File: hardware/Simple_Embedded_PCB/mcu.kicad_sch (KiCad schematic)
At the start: 26 parts, among them J1 USB_B_Micro, J2 SWD Connector, J3 Conn_01x09, J4 Conn_01x09, J5 Conn_01x09, J6 Conn_01x09, Q1 AO3400A, U1 STM32F103C8Tx, X1 SG-8018CE 8.000000MHz

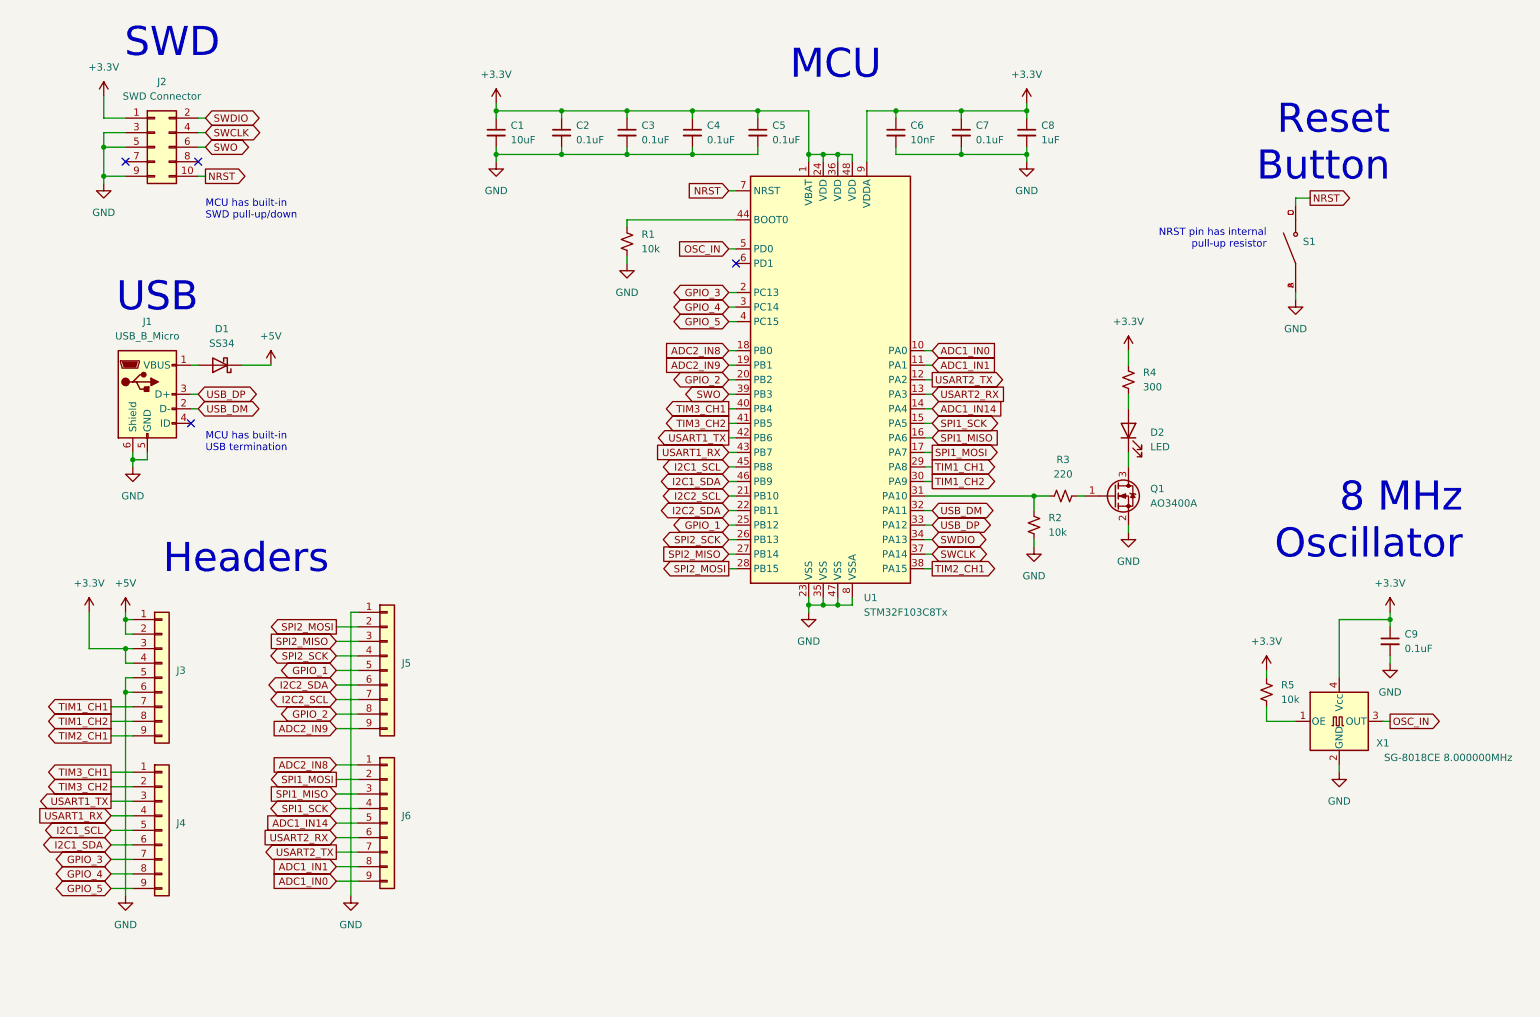
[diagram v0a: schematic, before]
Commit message: Added 4.7k pullups to I2C and reannotated
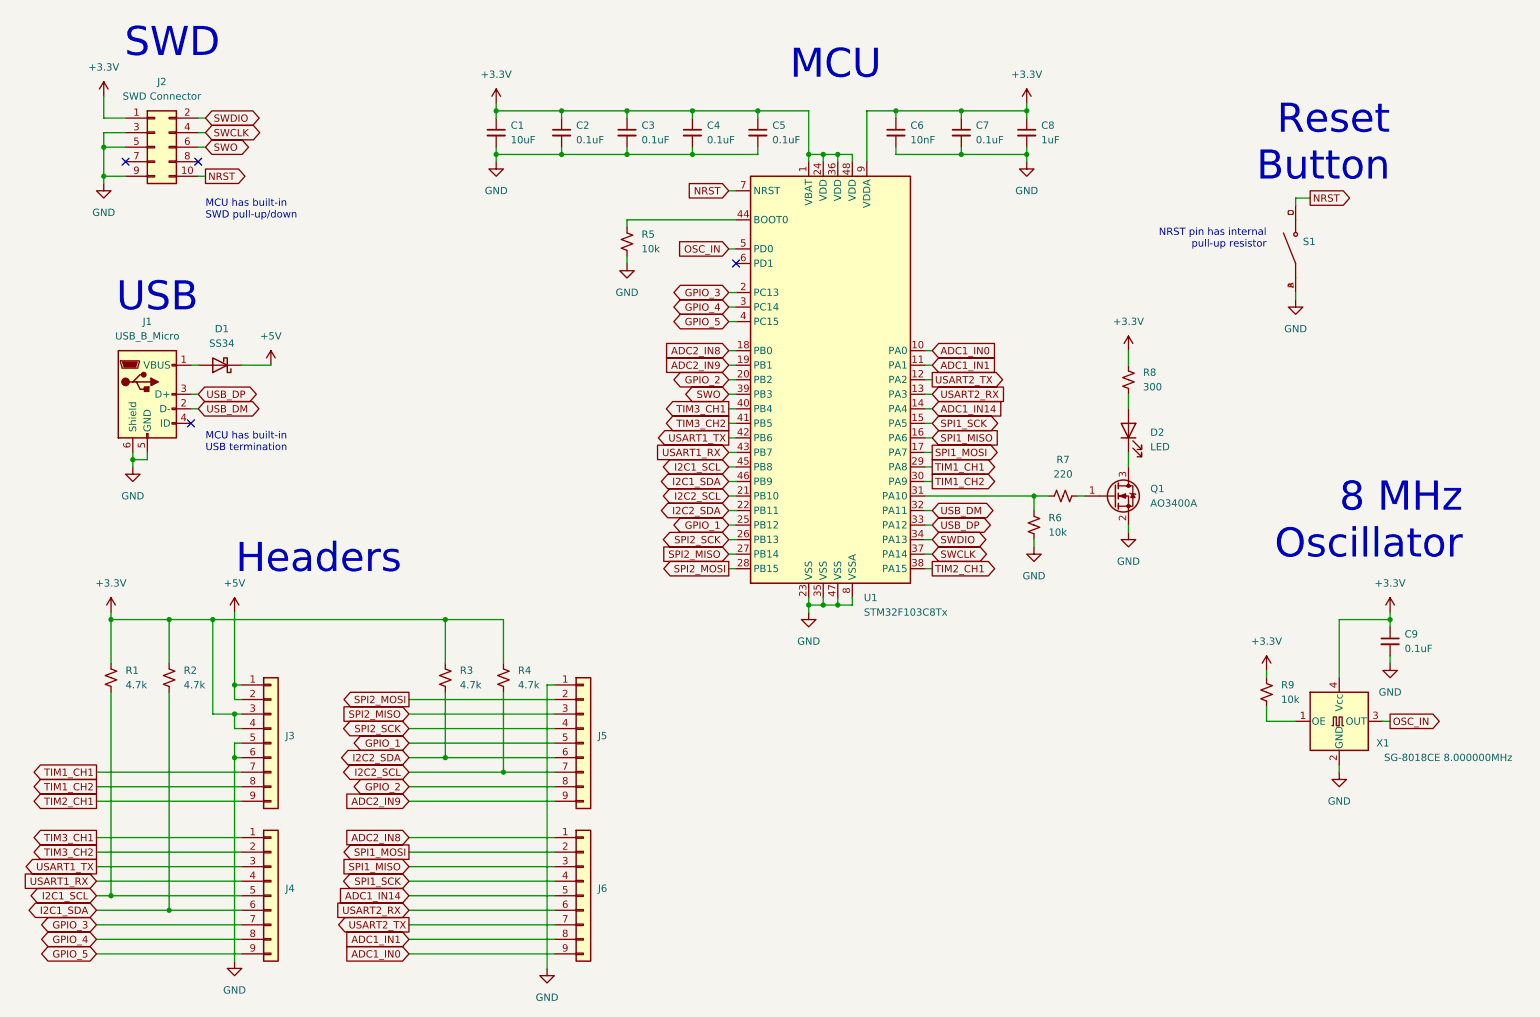
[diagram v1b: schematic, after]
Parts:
- added R1, R2, R3, R4: 4.7k, symbol Device:R_Small_US
- renumbered R1 to R5, R2 to R6, R3 to R7, R4 to R8, R5 to R9
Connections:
- net +3.3V: now also R1.1, R2.1, R3.1, R4.1
- net I2C1_SCL: now also R1.2
- net I2C1_SDA: now also R2.2
- net I2C2_SCL: now also R4.2
- net I2C2_SDA: now also R3.2
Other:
- moved on the sheet: J3, J4, J5, J6

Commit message: Preliminary layout done, removed resistors from PGOOD to just leave it floating
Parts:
- C1: footprint (none) -> Capacitor_SMD:C_0805_2012Metric
- C2, C3, C4, C5, C6, C7, C9: footprint (none) -> Capacitor_SMD:C_0402_1005Metric
- C8: footprint (none) -> Capacitor_SMD:C_0603_1608Metric
- R1, R2, R3, R4, R5, R6, R7, R9: footprint (none) -> Resistor_SMD:R_0402_1005Metric
- R8: footprint (none) -> Resistor_SMD:R_0603_1608Metric
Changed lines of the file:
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@@
       (effects (font (size 1.27 1.27)) (justify left))
     )
-    (property "Footprint" "" (id 2) (at 29.21 137.16 0)
+    (property "Footprint" "Resistor_SMD:R_0402_1005Metric" (id 2) (at 29.21 137.16 0)
       (effects (font (size 1.27 1.27)) hide)
     )
@@
       (effects (font (size 1.27 1.27)) (justify left))
     )
-    (property "Footprint" "" (id 2) (at 189.23 41.91 0)
+    (property "Footprint" "Capacitor_SMD:C_0603_1608Metric" (id 2) (at 189.23 41.91 0)
       (effects (font (size 1.27 1.27)) hide)
     )
@@
       (effects (font (size 1.27 1.27)) (justify left))
     )
-    (property "Footprint" "" (id 2) (at 87.63 137.16 0)
+    (property "Footprint" "Resistor_SMD:R_0402_1005Metric" (id 2) (at 87.63 137.16 0)
       (effects (font (size 1.27 1.27)) hide)
     )
@@
       (effects (font (size 1.27 1.27)) (justify left))
     )
-    (property "Footprint" "" (id 2) (at 252.73 130.81 0)
+    (property "Footprint" "Capacitor_SMD:C_0402_1005Metric" (id 2) (at 252.73 130.81 0)
       (effects (font (size 1.27 1.27)) hide)
     )
@@
       (effects (font (size 1.27 1.27)) (justify left))
     )
-    (property "Footprint" "" (id 2) (at 119.38 60.96 0)
+    (property "Footprint" "Resistor_SMD:R_0402_1005Metric" (id 2) (at 119.38 60.96 0)
       (effects (font (size 1.27 1.27)) hide)
     )
@@
       (effects (font (size 1.27 1.27)) (justify left))
     )
-    (property "Footprint" "" (id 2) (at 39.37 137.16 0)
+    (property "Footprint" "Resistor_SMD:R_0402_1005Metric" (id 2) (at 39.37 137.16 0)
       (effects (font (size 1.27 1.27)) hide)
     )
@@
       (effects (font (size 1.27 1.27)) (justify left))
     )
-    (property "Footprint" "" (id 2) (at 142.24 41.91 0)
+    (property "Footprint" "Capacitor_SMD:C_0402_1005Metric" (id 2) (at 142.24 41.91 0)
       (effects (font (size 1.27 1.27)) hide)
     )
@@
       (effects (font (size 1.27 1.27)) (justify left))
     )
-    (property "Footprint" "" (id 2) (at 190.5 110.49 0)
+    (property "Footprint" "Resistor_SMD:R_0402_1005Metric" (id 2) (at 190.5 110.49 0)
       (effects (font (size 1.27 1.27)) hide)
     )
@@
       (effects (font (size 1.27 1.27)) (justify left))
     )
-    (property "Footprint" "" (id 2) (at 96.52 41.91 0)
+    (property "Footprint" "Capacitor_SMD:C_0805_2012Metric" (id 2) (at 96.52 41.91 0)
       (effects (font (size 1.27 1.27)) hide)
     )
@@
       (effects (font (size 1.27 1.27)) (justify left))
     )
-    (property "Footprint" "" (id 2) (at 97.79 137.16 0)
+    (property "Footprint" "Resistor_SMD:R_0402_1005Metric" (id 2) (at 97.79 137.16 0)
       (effects (font (size 1.27 1.27)) hide)
     )
@@
       (effects (font (size 1.27 1.27)) (justify left))
     )
-    (property "Footprint" "" (id 2) (at 231.14 139.7 0)
+    (property "Footprint" "Resistor_SMD:R_0402_1005Metric" (id 2) (at 231.14 139.7 0)
       (effects (font (size 1.27 1.27)) hide)
     )
@@
       (effects (font (size 1.27 1.27)) (justify left))
     )
-    (property "Footprint" "" (id 2) (at 107.95 41.91 0)
+    (property "Footprint" "Capacitor_SMD:C_0402_1005Metric" (id 2) (at 107.95 41.91 0)
       (effects (font (size 1.27 1.27)) hide)
     )
@@
       (effects (font (size 1.27 1.27)) (justify right))
     )
-    (property "Footprint" "" (id 2) (at 207.01 85.09 0)
+    (property "Footprint" "Resistor_SMD:R_0603_1608Metric" (id 2) (at 207.01 85.09 0)
       (effects (font (size 1.27 1.27)) hide)
     )
@@
       (effects (font (size 1.27 1.27)) (justify left))
     )
-    (property "Footprint" "" (id 2) (at 119.38 41.91 0)
+    (property "Footprint" "Capacitor_SMD:C_0402_1005Metric" (id 2) (at 119.38 41.91 0)
       (effects (font (size 1.27 1.27)) hide)
     )
@@
       (effects (font (size 1.27 1.27)) (justify left))
     )
-    (property "Footprint" "" (id 2) (at 130.81 41.91 0)
+    (property "Footprint" "Capacitor_SMD:C_0402_1005Metric" (id 2) (at 130.81 41.91 0)
       (effects (font (size 1.27 1.27)) hide)
     )
@@
       (effects (font (size 1.27 1.27)) (justify left))
     )
-    (property "Footprint" "" (id 2) (at 166.37 41.91 0)
+    (property "Footprint" "Capacitor_SMD:C_0402_1005Metric" (id 2) (at 166.37 41.91 0)
       (effects (font (size 1.27 1.27)) hide)
     )
@@
     (property "Reference" "R7" (id 0) (at 195.58 99.06 90))
     (property "Value" "220" (id 1) (at 195.58 101.6 90))
-    (property "Footprint" "" (id 2) (at 195.58 105.41 0)
+    (property "Footprint" "Resistor_SMD:R_0402_1005Metric" (id 2) (at 195.58 105.41 0)
       (effects (font (size 1.27 1.27)) hide)
     )
@@
       (effects (font (size 1.27 1.27)) (justify left))
     )
-    (property "Footprint" "" (id 2) (at 177.8 41.91 0)
-      (effects (font (size 1.27 1.27)) hide)
-    )
+    (property "Footprint" "Capacitor_SMD:C_0402_1005Metric" (id 2) (at 177.8 41.91 0)
+      (effects (font (size 1.27 1.27)) hide)
+    )

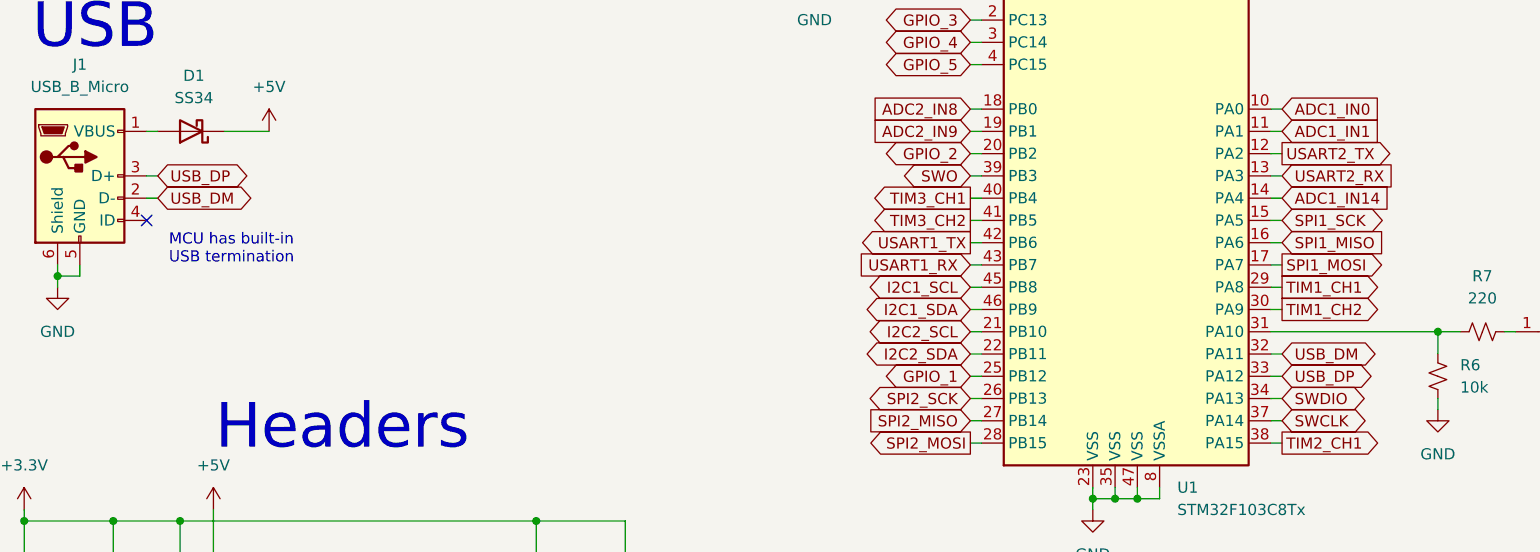
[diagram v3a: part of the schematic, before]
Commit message: Setup design rules and created proper board outline with mounting holes
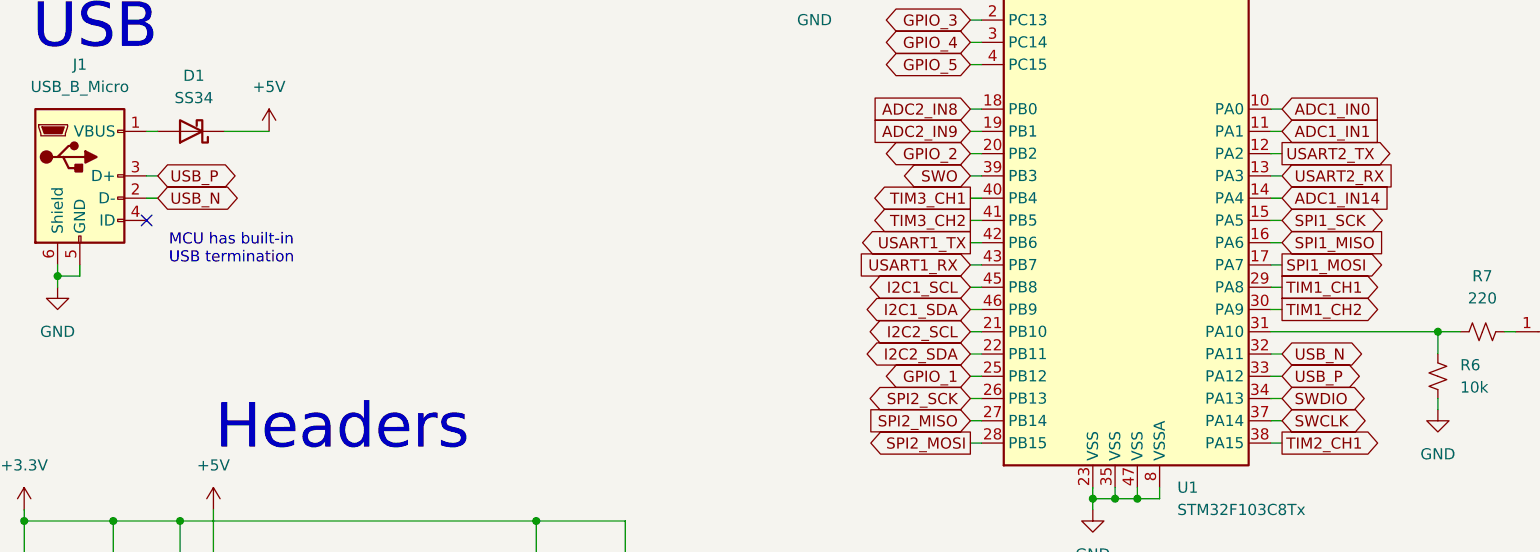
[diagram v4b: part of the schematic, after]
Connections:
- net USB_DM renamed USB_N
- net USB_DP renamed USB_P
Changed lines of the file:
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@@
     )
   )
-  (global_label "USB_DM" (shape bidirectional) (at 172.72 107.95 0) (fields_autoplaced)
+  (global_label "USB_N" (shape bidirectional) (at 172.72 107.95 0) (fields_autoplaced)
     (effects (font (size 1.27 1.27)) (justify left))
-    (property "Intersheet References" "${INTERSHEET_REFS}" (id 0) (at 182.6321 107.8706 0)
+    (property "Intersheet References" "${INTERSHEET_REFS}" (id 0) (at 181.2412 107.8706 0)
       (effects (font (size 1.27 1.27)) (justify left) hide)
     )
@@
     )
   )
-  (global_label "USB_DP" (shape bidirectional) (at 44.45 87.63 0) (fields_autoplaced)
+  (global_label "USB_P" (shape bidirectional) (at 44.45 87.63 0) (fields_autoplaced)
     (effects (font (size 1.27 1.27)) (justify left))
-    (property "Intersheet References" "${INTERSHEET_REFS}" (id 0) (at 54.1807 87.5506 0)
+    (property "Intersheet References" "${INTERSHEET_REFS}" (id 0) (at 52.9107 87.5506 0)
       (effects (font (size 1.27 1.27)) (justify left) hide)
     )
@@
     )
   )
-  (global_label "USB_DP" (shape bidirectional) (at 172.72 110.49 0) (fields_autoplaced)
+  (global_label "USB_P" (shape bidirectional) (at 172.72 110.49 0) (fields_autoplaced)
     (effects (font (size 1.27 1.27)) (justify left))
-    (property "Intersheet References" "${INTERSHEET_REFS}" (id 0) (at 182.4507 110.4106 0)
+    (property "Intersheet References" "${INTERSHEET_REFS}" (id 0) (at 181.1807 110.4106 0)
       (effects (font (size 1.27 1.27)) (justify left) hide)
     )
@@
     )
   )
-  (global_label "USB_DM" (shape bidirectional) (at 44.45 90.17 0) (fields_autoplaced)
+  (global_label "USB_N" (shape bidirectional) (at 44.45 90.17 0) (fields_autoplaced)
     (effects (font (size 1.27 1.27)) (justify left))
-    (property "Intersheet References" "${INTERSHEET_REFS}" (id 0) (at 54.3621 90.0906 0)
+    (property "Intersheet References" "${INTERSHEET_REFS}" (id 0) (at 52.9712 90.0906 0)
       (effects (font (size 1.27 1.27)) (justify left) hide)
     )

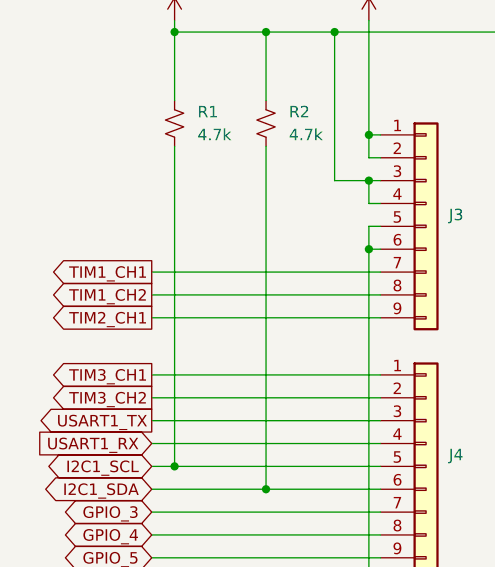
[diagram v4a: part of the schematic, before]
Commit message: Routed all PCB traces, began routing power
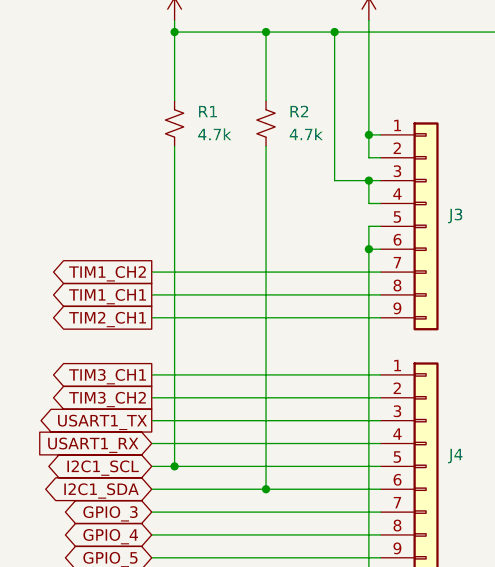
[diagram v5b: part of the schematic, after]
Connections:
- net TIM1_CH1: now also J3.8 (Pin_8); no longer J3.7 (Pin_7)
- net TIM1_CH2: now also J3.7 (Pin_7); no longer J3.8 (Pin_8)
